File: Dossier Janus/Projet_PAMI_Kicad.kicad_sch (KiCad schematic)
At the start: 33 parts, among them U2 MCU

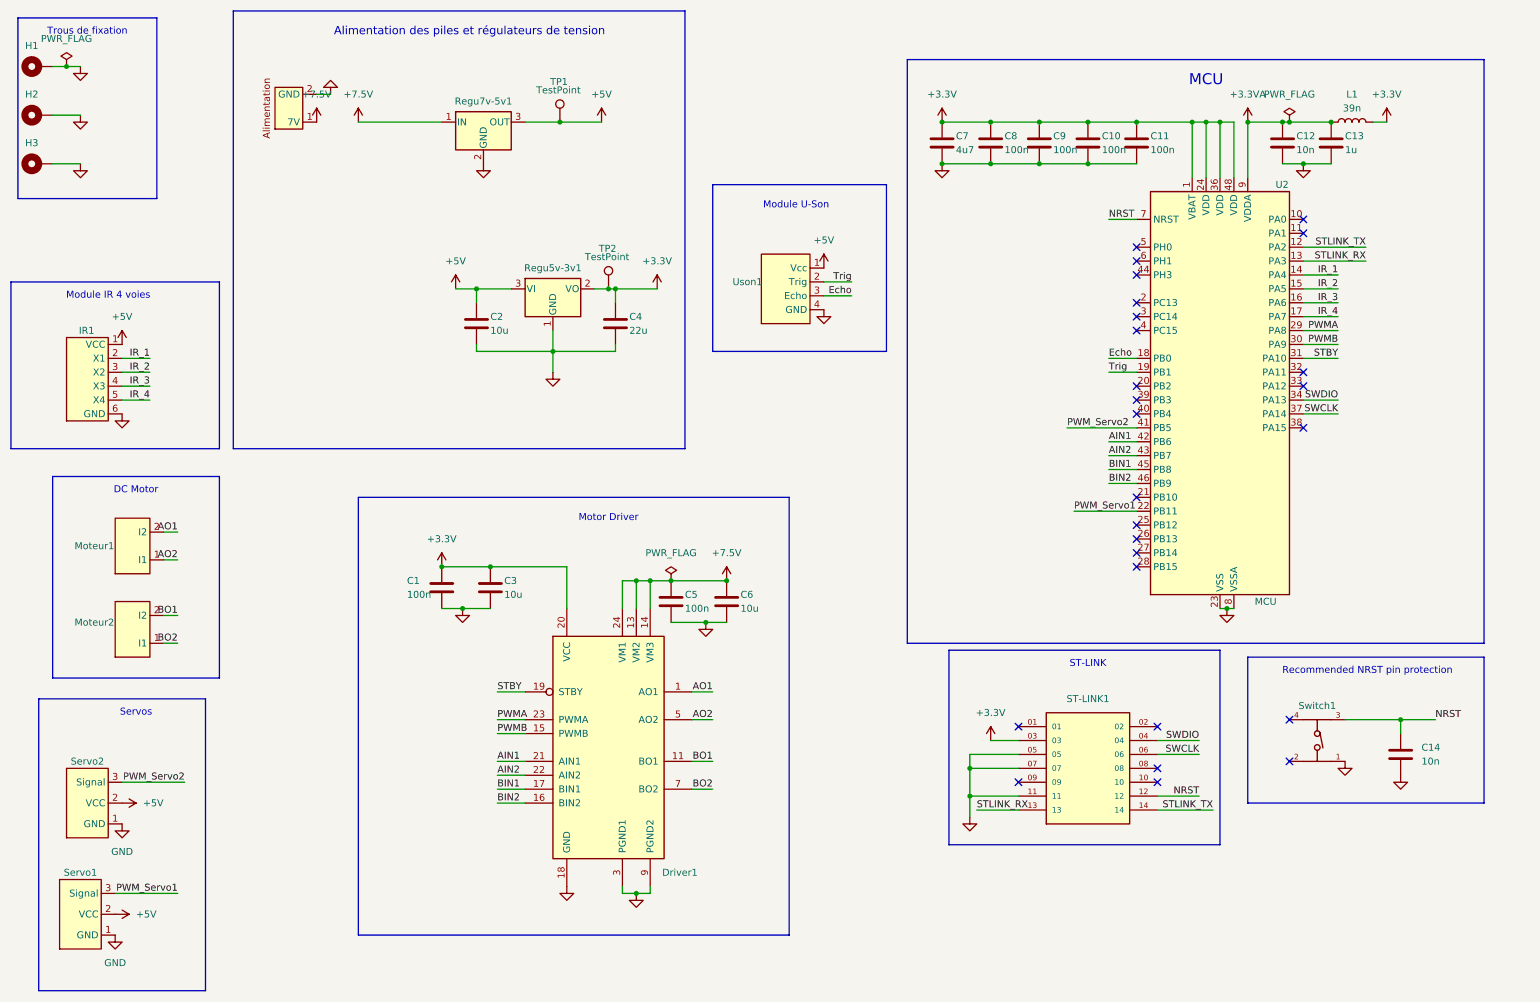
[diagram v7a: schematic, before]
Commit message: ajout du répertoire Dossier Janus-bis contenant la version finale du PCB
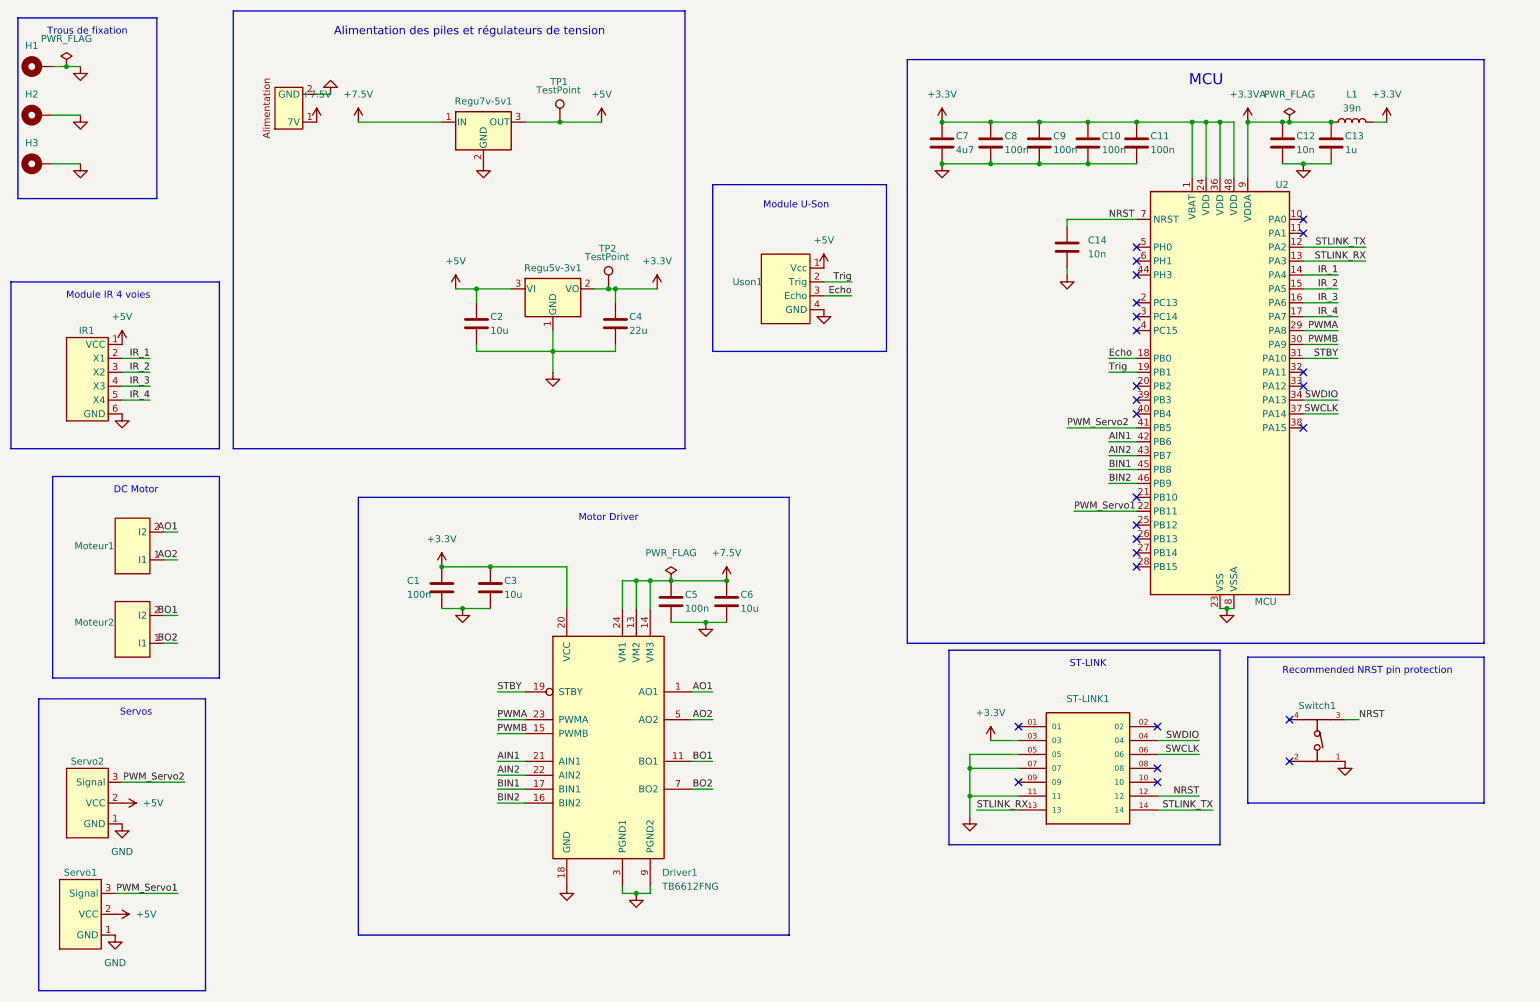
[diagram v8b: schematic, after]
